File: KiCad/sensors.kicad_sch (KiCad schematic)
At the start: 26 parts, among them Q1 AO3401A, U4 GXHTC3, U5 LTR-303ALS-01

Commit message: gerber power changed
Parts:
- TP10, TP11, TP12, TP13, TP7, TP8, TP9: footprint TestPoint:TestPoint_Loop_D2.54mm_Drill1.5mm_Beaded -> footprint:Testpoint_2.54mm
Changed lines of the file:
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@@
       (effects (font (size 1.27 1.27)) (justify left))
     )
-    (property "Footprint" "TestPoint:TestPoint_Loop_D2.54mm_Drill1.5mm_Beaded" (at 186.69 40.64 0)
+    (property "Footprint" "footprint:Testpoint_2.54mm" (at 186.69 40.64 0)
       (effects (font (size 1.27 1.27)) hide)
     )
@@
       (effects (font (size 1.27 1.27)) (justify left))
     )
-    (property "Footprint" "TestPoint:TestPoint_Loop_D2.54mm_Drill1.5mm_Beaded" (at 186.69 45.72 0)
+    (property "Footprint" "footprint:Testpoint_2.54mm" (at 186.69 45.72 0)
       (effects (font (size 1.27 1.27)) hide)
     )
@@
       (effects (font (size 1.27 1.27)) (justify left))
     )
-    (property "Footprint" "TestPoint:TestPoint_Loop_D2.54mm_Drill1.5mm_Beaded" (at 186.69 35.56 0)
+    (property "Footprint" "footprint:Testpoint_2.54mm" (at 186.69 35.56 0)
       (effects (font (size 1.27 1.27)) hide)
     )
@@
       (effects (font (size 1.27 1.27)) (justify left))
     )
-    (property "Footprint" "TestPoint:TestPoint_Loop_D2.54mm_Drill1.5mm_Beaded" (at 134.62 52.07 0)
+    (property "Footprint" "footprint:Testpoint_2.54mm" (at 134.62 52.07 0)
       (effects (font (size 1.27 1.27)) hide)
     )
@@
       (effects (font (size 1.27 1.27)) (justify left))
     )
-    (property "Footprint" "TestPoint:TestPoint_Loop_D2.54mm_Drill1.5mm_Beaded" (at 189.23 92.71 0)
+    (property "Footprint" "footprint:Testpoint_2.54mm" (at 189.23 92.71 0)
       (effects (font (size 1.27 1.27)) hide)
     )
@@
       (effects (font (size 1.27 1.27)) (justify left))
     )
-    (property "Footprint" "TestPoint:TestPoint_Loop_D2.54mm_Drill1.5mm_Beaded" (at 139.7 107.95 0)
+    (property "Footprint" "footprint:Testpoint_2.54mm" (at 139.7 107.95 0)
       (effects (font (size 1.27 1.27)) hide)
     )
@@
       (effects (font (size 1.27 1.27)) (justify left))
     )
-    (property "Footprint" "TestPoint:TestPoint_Loop_D2.54mm_Drill1.5mm_Beaded" (at 189.23 97.79 0)
-      (effects (font (size 1.27 1.27)) hide)
-    )
+    (property "Footprint" "footprint:Testpoint_2.54mm" (at 189.23 97.79 0)
+      (effects (font (size 1.27 1.27)) hide)
+    )

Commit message: lots of PCB stuff
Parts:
- removed TP12: TempHum SDA, footprint:Testpoint_2.54mm, symbol Connector:TestPoint
- removed TP13: TempHum SCL, footprint:Testpoint_2.54mm, symbol Connector:TestPoint
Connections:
- net +3.3V renamed +3V3

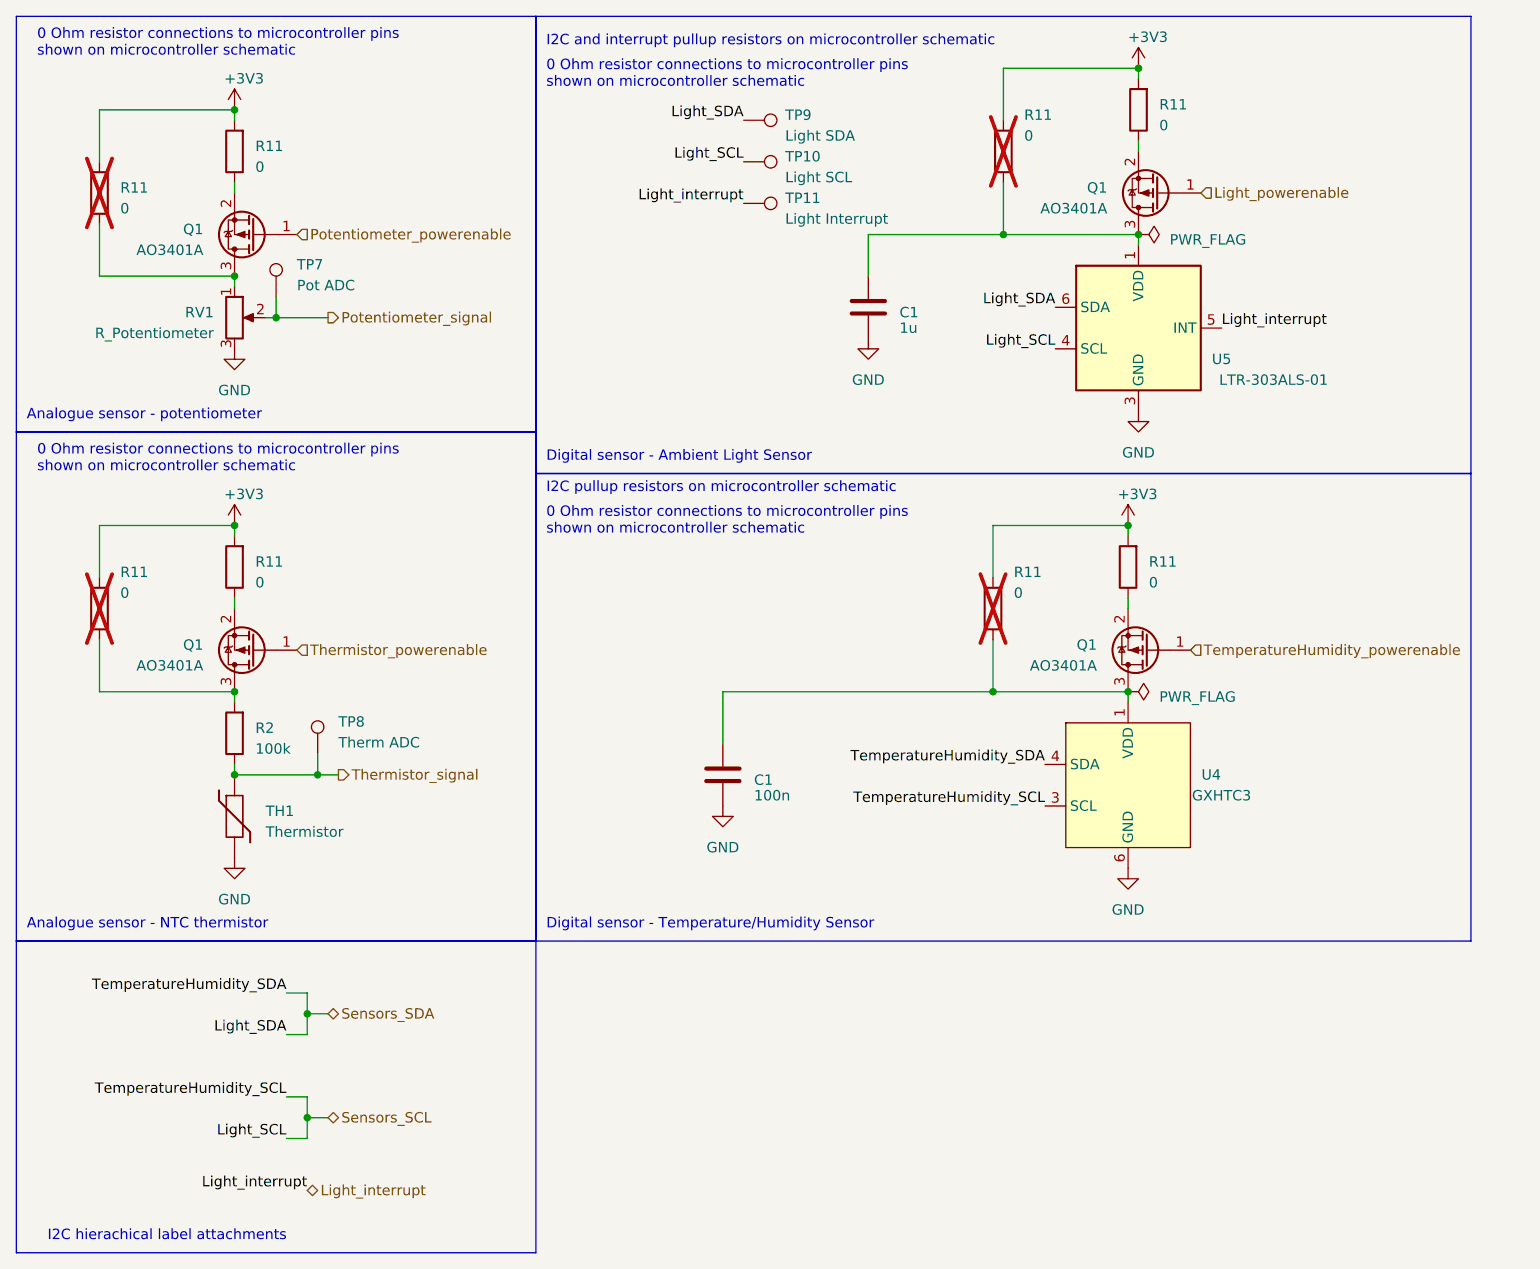
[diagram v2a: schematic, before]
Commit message: powwer 5v line seperation
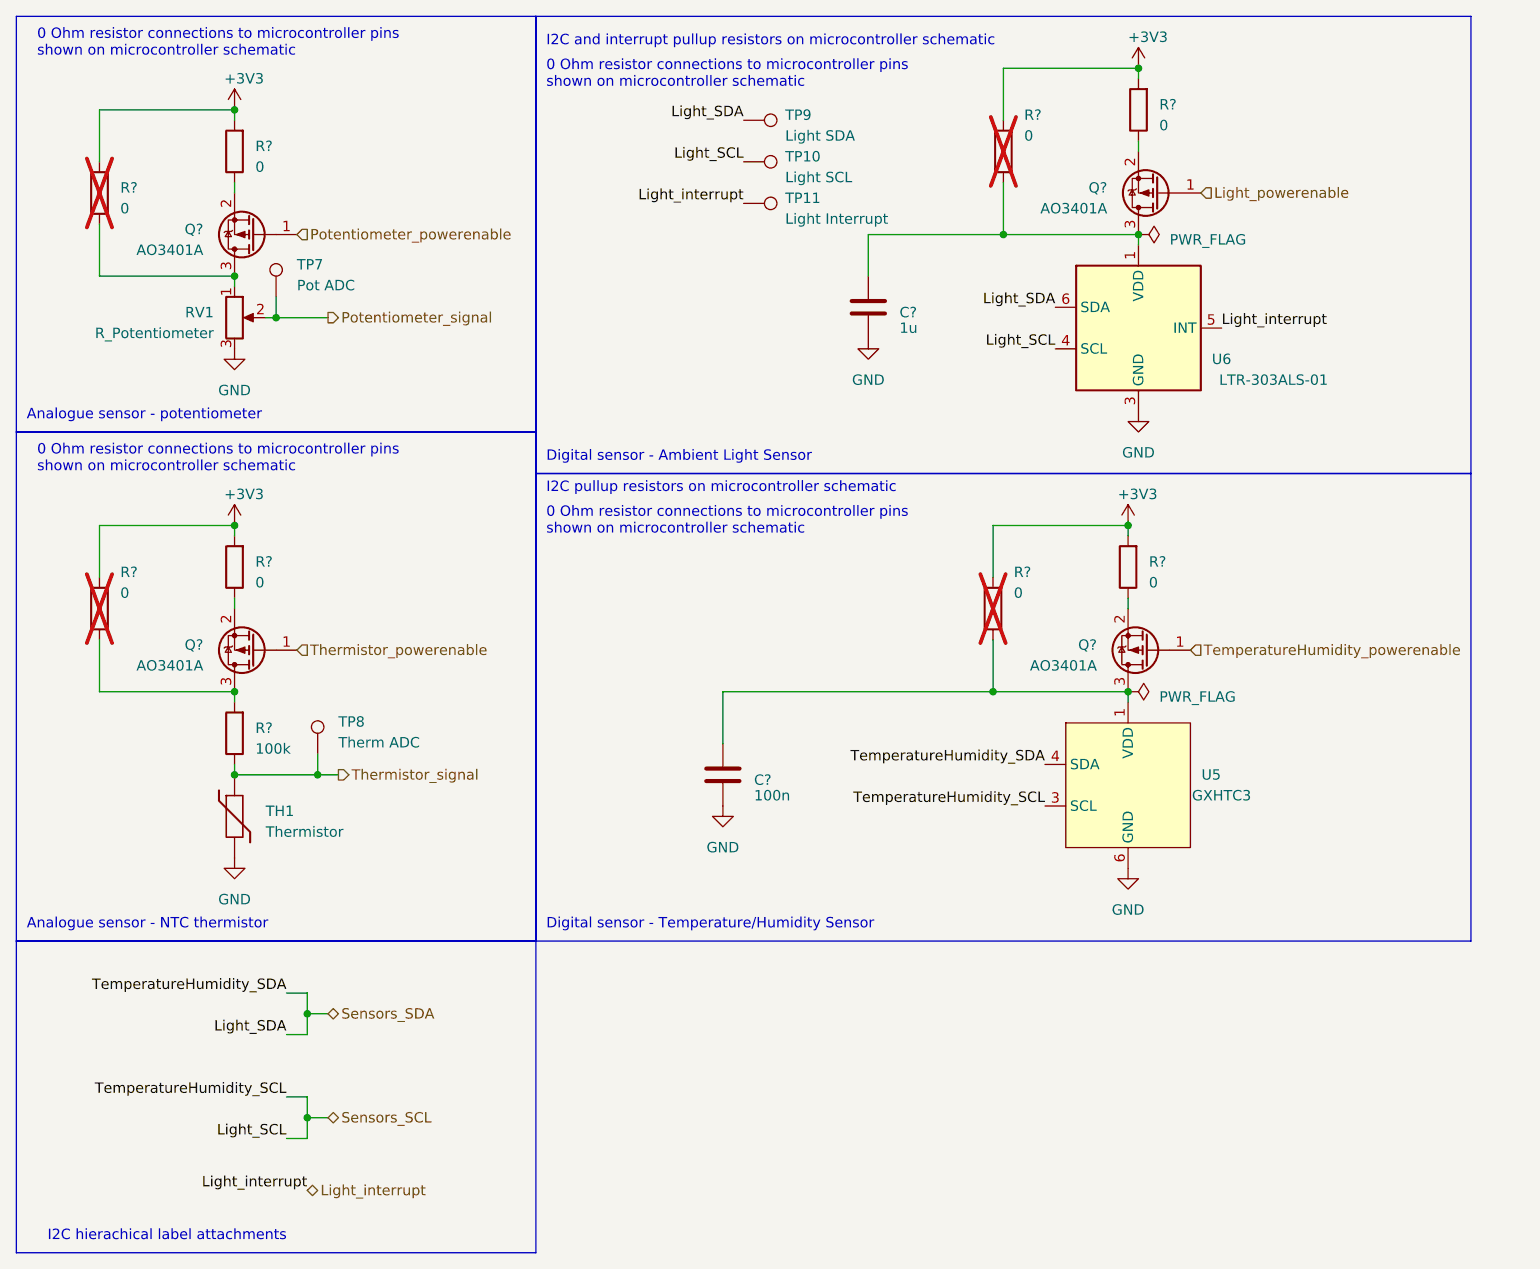
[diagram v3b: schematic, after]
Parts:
- renumbered C1 to C?, Q1 to Q?, R11 to R?, R2 to R?, U4 to U5, U5 to U6

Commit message: any residual changes from previous commit
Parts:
- TP10: value Light SCL -> Sensors SCL
- TP9: value Light SDA -> Sensors SDA
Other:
- moved on the sheet: TP10, TP9
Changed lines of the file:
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@@
   (junction (at 129.54 54.61) (diameter 0) (color 0 0 0 0)
   )
+  (junction (at 233.68 80.01) (diameter 0) (color 0 0 0 0)
+  )
   (junction (at 133.35 139.7) (diameter 0) (color 0 0 0 0)
   )
-  (junction (at 233.68 80.01) (diameter 0) (color 0 0 0 0)
-  )
   (junction (at 233.68 100.33) (diameter 0) (color 0 0 0 0)
   )
@@
   (junction (at 218.44 44.45) (diameter 0) (color 0 0 0 0)
   )
+  (junction (at 133.35 149.86) (diameter 0) (color 0 0 0 0)
+  )
   (junction (at 124.46 110.49) (diameter 0) (color 0 0 0 0)
   )
+  (junction (at 133.35 137.16) (diameter 0) (color 0 0 0 0)
+  )
   (junction (at 134.62 110.49) (diameter 0) (color 0 0 0 0)
   )
@@
   )
   (wire (pts (xy 107.95 80.01) (xy 124.46 80.01))
-    (stroke (width 0) (type default))
-  )
-  (wire (pts (xy 233.68 79.502) (xy 233.68 80.01))
     (stroke (width 0) (type default))
   )
@@
     (effects (font (size 1.27 1.27)) (justify right bottom))
   )
-  (label "Light_SDA" (at 186.69 30.48 180) (fields_autoplaced)
-    (effects (font (size 1.27 1.27)) (justify right bottom))
-  )
   (label "Light_SCL" (at 224.79 58.42 180) (fields_autoplaced)
     (effects (font (size 1.27 1.27)) (justify right bottom))
@@
     (effects (font (size 1.27 1.27)) (justify right bottom))
   )
-  (label "Light_SCL" (at 186.69 35.56 180) (fields_autoplaced)
-    (effects (font (size 1.27 1.27)) (justify right bottom))
-  )
   (label "Light_interrupt" (at 133.35 161.29 180) (fields_autoplaced)
     (effects (font (size 1.27 1.27)) (justify right bottom))
@@
     (effects (font (size 1.27 1.27)) (justify left))
   )
-  (symbol (lib_id "Connector:TestPoint") (at 186.69 35.56 270) (unit 1)
+  (symbol (lib_id "Connector:TestPoint") (at 133.35 149.86 0) (unit 1)
     (in_bom yes) (on_board yes) (dnp no) (fields_autoplaced)
-    (property "Reference" "TP10" (at 191.77 34.925 90)
-      (effects (font (size 1.27 1.27)) (justify left))
-    )
-    (property "Value" "Light SCL" (at 191.77 37.465 90)
-      (effects (font (size 1.27 1.27)) (justify left))
-    )
-    (property "Footprint" "footprint:Testpoint_2.54mm" (at 186.69 40.64 0)
-      (effects (font (size 1.27 1.27)) hide)
-    )
-    (property "Datasheet" "~" (at 186.69 40.64 0)
-      (effects (font (size 1.27 1.27)) hide)
-    )
-    (property "Extended Part Cost" "0" (at 186.69 35.56 0)
-      (effects (font (size 1.27 1.27)) hide)
-    )
-    (property "cost per unit" "0" (at 186.69 35.56 0)
+    (property "Reference" "TP10" (at 135.89 145.923 0)
+      (effects (font (size 1.27 1.27)) (justify left))
+    )
+    (property "Value" "Sensors SCL" (at 135.89 148.463 0)
+      (effects (font (size 1.27 1.27)) (justify left))
+    )
+    (property "Footprint" "footprint:Testpoint_2.54mm" (at 138.43 149.86 0)
+      (effects (font (size 1.27 1.27)) hide)
+    )
+    (property "Datasheet" "~" (at 138.43 149.86 0)
+      (effects (font (size 1.27 1.27)) hide)
+    )
+    (property "Extended Part Cost" "0" (at 133.35 149.86 0)
+      (effects (font (size 1.27 1.27)) hide)
+    )
+    (property "cost per unit" "0" (at 133.35 149.86 0)
       (effects (font (size 1.27 1.27)) hide)
     )
@@
     )
   )
-  (symbol (lib_id "Connector:TestPoint") (at 186.69 30.48 270) (unit 1)
+  (symbol (lib_id "Connector:TestPoint") (at 133.35 137.16 0) (unit 1)
     (in_bom yes) (on_board yes) (dnp no) (fields_autoplaced)
-    (property "Reference" "TP9" (at 191.77 29.845 90)
-      (effects (font (size 1.27 1.27)) (justify left))
-    )
-    (property "Value" "Light SDA" (at 191.77 32.385 90)
-      (effects (font (size 1.27 1.27)) (justify left))
-    )
-    (property "Footprint" "footprint:Testpoint_2.54mm" (at 186.69 35.56 0)
-      (effects (font (size 1.27 1.27)) hide)
-    )
-    (property "Datasheet" "~" (at 186.69 35.56 0)
-      (effects (font (size 1.27 1.27)) hide)
-    )
-    (property "Extended Part Cost" "0" (at 186.69 30.48 0)
-      (effects (font (size 1.27 1.27)) hide)
-    )
-    (property "cost per unit" "0" (at 186.69 30.48 0)
-      (effects (font (size 1.27 1.27)) hide)
-    )
+    (property "Reference" "TP9" (at 135.89 133.223 0)
+      (effects (font (size 1.27 1.27)) (justify left))
+    )
+    (property "Value" "Sensors SDA" (at 135.89 135.763 0)
+      (effects (font (size 1.27 1.27)) (justify left))
+    )
+    (property "Footprint" "footprint:Testpoint_2.54mm" (at 138.43 137.16 0)
+      (effects (font (size 1.27 1.27)) hide)
+    )
+    (property "Datasheet" "~" (at 138.43 137.16 0)
+      (effects (font (size 1.27 1.27)) hide)
+    )
+    (property "Extended Part Cost" "0" (at 133.35 137.16 0)
+      (effects (font (size 1.27 1.27)) hide)
+    )
+    (property "cost per unit" "0" (at 133.35 137.16 0)
+      (effects (font (size 1.27 1.27)) hide)
+    )

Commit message: Corrected all part numbers and small schematic changes
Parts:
- Q? (x4): cost per unit 0,0797 -> 0,07965
- TH1: cost per unit 0.0130 -> 0.0126
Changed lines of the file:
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@@
       (effects (font (size 1.27 1.27)) hide)
     )
-    (property "cost per unit" "0,0797" (at 236.22 95.25 0)
+    (property "cost per unit" "0,07965" (at 236.22 95.25 0)
       (effects (font (size 1.27 1.27)) hide)
     )
@@
       (effects (font (size 1.27 1.27)) hide)
     )
-    (property "cost per unit" "0,0797" (at 127 95.25 0)
+    (property "cost per unit" "0,07965" (at 127 95.25 0)
       (effects (font (size 1.27 1.27)) hide)
     )
@@
       (effects (font (size 1.27 1.27)) hide)
     )
-    (property "cost per unit" "0,0797" (at 237.49 39.37 0)
+    (property "cost per unit" "0,07965" (at 237.49 39.37 0)
       (effects (font (size 1.27 1.27)) hide)
     )
@@
       (effects (font (size 1.27 1.27)) hide)
     )
-    (property "cost per unit" "0,0797" (at 127 44.45 0)
+    (property "cost per unit" "0,07965" (at 127 44.45 0)
       (effects (font (size 1.27 1.27)) hide)
     )
@@
       (effects (font (size 1.27 1.27)) hide)
     )
-    (property "cost per unit" "0.0130" (at 124.46 115.57 0)
-      (effects (font (size 1.27 1.27)) hide)
-    )
+    (property "cost per unit" "0.0126" (at 124.46 115.57 0)
+      (effects (font (size 1.27 1.27)) hide)
+    )

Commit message: Final schematic changes and start board design
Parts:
- C?: footprint footprint:C0402 -> JLCPartFootprints:C0402
- C?: footprint footprint:C0402_NEW -> JLCPartFootprints:C0402
- Q? (x4): footprint footprint:SOT-23_L2.9-W1.3-P1.90-LS2.4-BR -> JLCPartFootprints:SOT-23_L2.9-W1.3-P1.90-LS2.4-BR
- R? (x8): footprint footprint:R0603 -> JLCPartFootprints:R0603
- R?: footprint footprint:R1206 -> JLCPartFootprints:R1206
- RV1: footprint footprint:RES-ADJ-TH_RK09K1130AJ3 -> JLCPartFootprints:RES-ADJ-TH_RK09K1130AJ3
- TH1: footprint footprint:R0402 -> JLCPartFootprints:R0402
- TP10: renamed from TP11; footprint footprint:Testpoint_2.54mm -> CustomFootprints:Testpoint; DNF (none) -> X
- TP6: renamed from TP7; footprint footprint:Testpoint_2.54mm -> CustomFootprints:Testpoint; DNF (none) -> X
- TP7: renamed from TP9; footprint footprint:Testpoint_2.54mm -> CustomFootprints:Testpoint; DNF (none) -> X
- TP8: renamed from TP10; footprint footprint:Testpoint_2.54mm -> CustomFootprints:Testpoint; DNF (none) -> X
- TP9: renamed from TP8; footprint footprint:Testpoint_2.54mm -> CustomFootprints:Testpoint; DNF (none) -> X
- U5: footprint footprint:DFN-6_L2.0-W2.0-P0.50-BL-EP -> JLCPartFootprints:DFN-6_L2.0-W2.0-P0.50-BL-EP
- U6: footprint footprint:SOT-363_L2.0-W1.3-P0.65-LS2.1-BL -> JLCPartFootprints:SOT-363_L2.0-W1.3-P0.65-LS2.1-BL
